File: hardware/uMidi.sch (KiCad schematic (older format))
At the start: 61 parts, among them CON1 USB-MINI-B, IC1 ATXMEGA128A4U-M, IC2 74LS14, IC3 LT1129CST-3.3, IC4 6N138, P1 MIDI In, P2 MIDI Thru, P3 MIDI T/O, P4 MIDI Out, P5 5..12 V, P6 PDI, P7 GPIO1, P8 GPIO2, P9 GPIO3

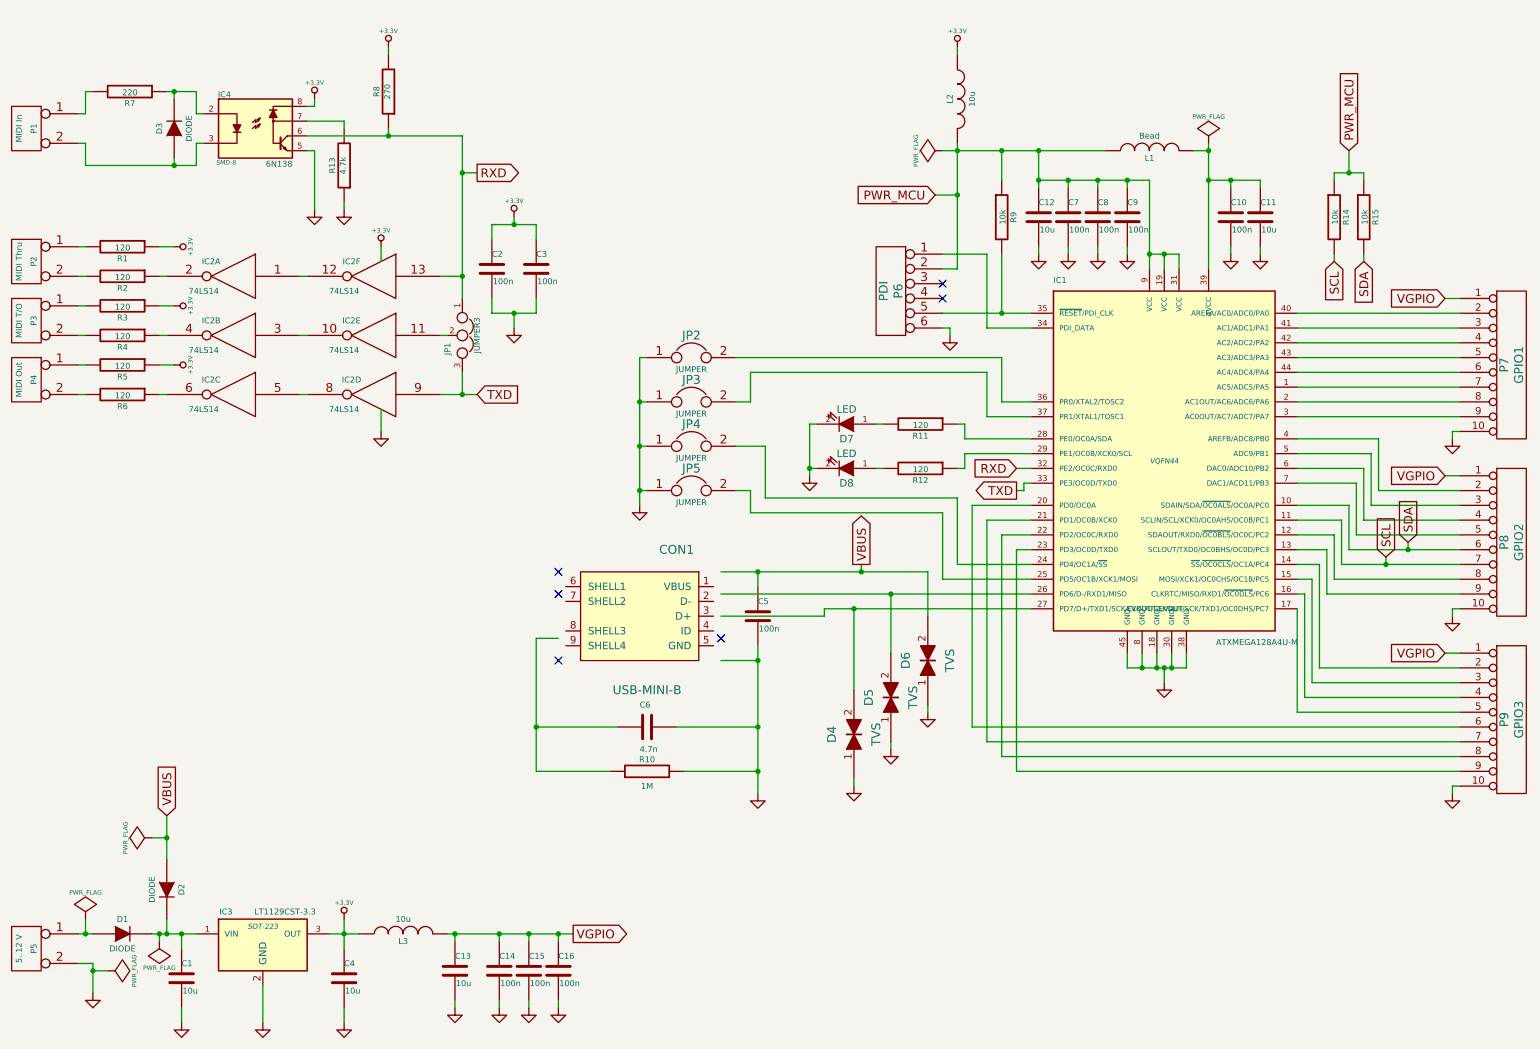
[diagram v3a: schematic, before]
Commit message: Fix usb connector in schematic
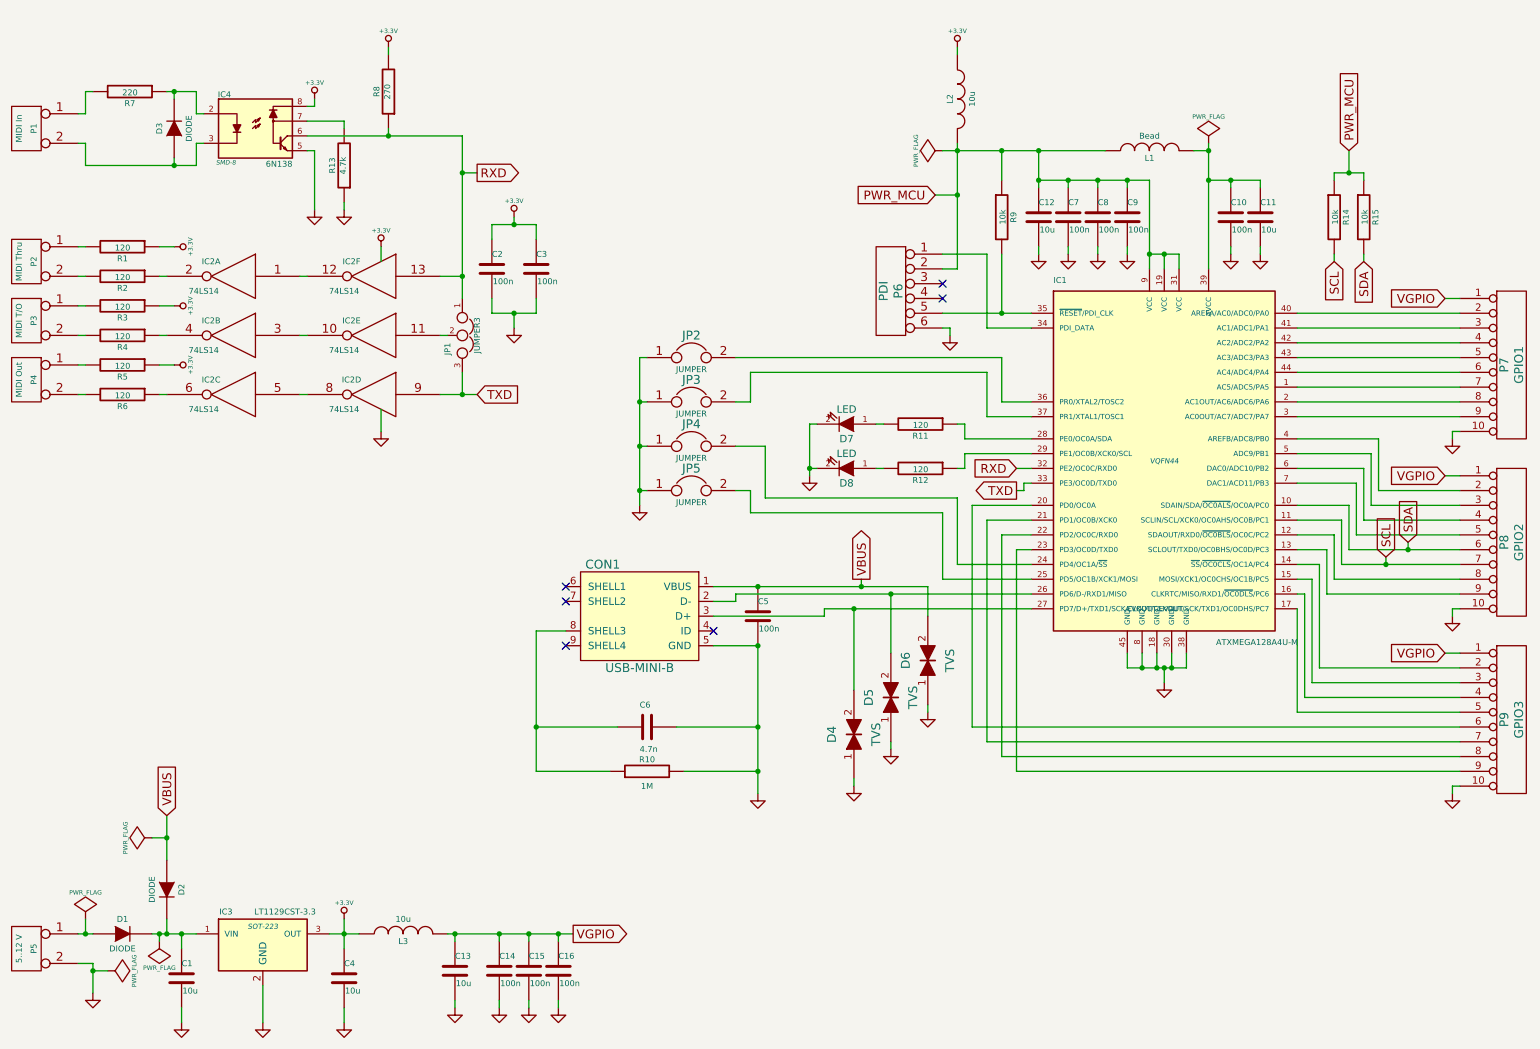
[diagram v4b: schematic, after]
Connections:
- net GND: now also CON1.5 (GND)
- net VBUS: now also CON1.1 (VBUS)
- net at D5.2, IC1.26 (PD6/D-/RXD1/MISO): now also CON1.2 (D-)
- net at D4.2, IC1.27 (PD7/D+/TXD1/SCK/CLKOUT/EVOUT): now also CON1.3 (D+)
- net at CON1.8 (SHELL3): now also C6.2, R10.1
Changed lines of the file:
@@
 U 1 1 53C6D9DB
 P 4950 4600
-F 0 "CON1" H 4700 5050 60  0000 C CNN
-F 1 "USB-MINI-B" H 4900 4100 60  0000 C CNN
+F 0 "CON1" H 5200 4950 60  0000 C CNN
+F 1 "USB-MINI-B" H 4950 4250 60  0000 C CNN
 F 2 "" H 4950 4600 60  0000 C CNN
 F 3 "" H 4950 4600 60  0000 C CNN
@@
 	1    0    0    -1
 $EndComp
-Text GLabel 6450 4250 1    60   Output ~ 0
+Text GLabel 6450 4350 1    60   Output ~ 0
 VBUS
 Text GLabel 1750 5950 1    60   Input ~ 0
@@
 	1    0    0    -1
 $EndComp
-NoConn ~ 5500 4750
+NoConn ~ 5450 4700
 $Comp
 L PWR_FLAG #FLG032
@@
 	6200 4550 7600 4550
 Wire Wire Line
-	5500 4450 7600 4450
+	5600 4450 7600 4450
 Wire Wire Line
 	3750 2950 3750 3100
@@
 	6200 4600 6200 4550
 Wire Wire Line
-	5500 4600 6200 4600
-Wire Wire Line
-	5500 4900 5750 4900
-Wire Wire Line
-	6450 4300 6450 4250
+	5450 4600 6200 4600
+Wire Wire Line
+	5450 4800 5750 4800
+Wire Wire Line
+	6450 4400 6450 4350
 Wire Wire Line
 	7600 4150 7500 4150
@@
 Wire Wire Line
 	7050 2650 7050 2700
-Connection ~ 6450 4300
+Connection ~ 6450 4400
 Connection ~ 6650 4450
 Connection ~ 6400 4550
@@
 	6650 4450 6650 4850
 Wire Wire Line
-	6900 4300 6900 4600
+	6900 4400 6900 4600
 Wire Wire Line
 	5750 4800 5750 5800
-Connection ~ 5750 4900
-Wire Wire Line
-	5750 4400 5750 4300
-Connection ~ 5750 4300
+Connection ~ 5750 4800
+Wire Wire Line
+	5450 4400 6900 4400
+Connection ~ 5750 4400
 Wire Wire Line
 	1250 7000 1350 7000
@@
 	3200 2100 3200 2200
 Wire Wire Line
-	4400 4750 4250 4750
-Wire Wire Line
-	4250 4750 4250 5650
+	4250 4700 4250 5650
 Wire Wire Line
 	4250 5350 4800 5350
@@
 Wire Wire Line
 	9750 1600 9750 1450
-Wire Wire Line
-	5500 4300 6900 4300
-NoConn ~ 4400 4300
-NoConn ~ 4400 4450
-NoConn ~ 4400 4900
+NoConn ~ 4450 4400
+NoConn ~ 4450 4500
+NoConn ~ 4450 4800
 Wire Wire Line
 	3600 3100 3850 3100
@@
 	3600 2300 3750 2300
 Wire Wire Line
-	3750 1350 2700 1350
+	2700 1350 3750 1350
 $Comp
 L JUMPER JP2
@@
 $EndComp
 Wire Wire Line
-	4950 3850 4950 2850
+	4950 2850 4950 3850
 Wire Wire Line
 	4950 2850 5000 2850
@@
 Wire Wire Line
 	5800 3450 5600 3450
+Wire Wire Line
+	4250 4700 4450 4700
+Wire Wire Line
+	5600 4450 5600 4500
+Wire Wire Line
+	5600 4500 5450 4500
 $EndSCHEMATC

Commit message: Rescue symbols to work with kicad bzr 6188
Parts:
- C1, C10, C11, C12, C13, C14, C15, C16, C2, C3, C4, C5, C6, C7, C8, C9: symbol C -> C-RESCUE-uMidi
- D7, D8: symbol LED -> LED-RESCUE-uMidi
- IC4: symbol 6N135 -> 6N135-RESCUE-uMidi
- R1, R10, R11, R12, R13, R14, R15, R2, R3, R4, R5, R6, R7, R8, R9: symbol R -> R-RESCUE-uMidi
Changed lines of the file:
@@
 EESchema Schematic File Version 2
+LIBS:uMidi-rescue
 LIBS:power
 LIBS:device
@@
 LIBS:memory
 LIBS:xilinx
-LIBS:special
 LIBS:microcontrollers
 LIBS:dsp
@@
 LIBS:atmel
 LIBS:uMidi-cache
-EELAYER 24 0
+EELAYER 25 0
 EELAYER END
 $Descr A4 11693 8268
@@
 $EndComp
 $Comp
-L +3.3V #PWR02
+L +3.3V-RESCUE-uMidi #PWR02
 U 1 1 53C6C3CA
 P 7100 750
@@
 $EndComp
 $Comp
-L R R9
+L R-RESCUE-uMidi R9
 U 1 1 53C6C462
 P 7400 1900
@@
 $EndComp
 $Comp
-L +3.3V #PWR05
+L +3.3V-RESCUE-uMidi #PWR05
 U 1 1 53C6D766
 P 3200 2100
@@
 $EndComp
 $Comp
-L R R2
+L R-RESCUE-uMidi R2
 U 1 1 53C9474B
 P 1450 2300
@@
 $EndComp
 $Comp
-L R R4
+L R-RESCUE-uMidi R4
 U 1 1 53C94767
 P 1450 2700
@@
 $EndComp
 $Comp
-L R R6
+L R-RESCUE-uMidi R6
 U 1 1 53C94772
 P 1450 3100
@@
 $EndComp
 $Comp
-L R R1
+L R-RESCUE-uMidi R1
 U 1 1 53C9484F
 P 1450 2100
@@
 $EndComp
 $Comp
-L R R3
+L R-RESCUE-uMidi R3
 U 1 1 53C9485A
 P 1450 2500
@@
 $EndComp
 $Comp
-L R R5
+L R-RESCUE-uMidi R5
 U 1 1 53C94865
 P 1450 2900
@@
 $EndComp
 $Comp
-L +3.3V #PWR07
+L +3.3V-RESCUE-uMidi #PWR07
 U 1 1 53C94936
 P 1800 2100
@@
 $EndComp
 $Comp
-L +3.3V #PWR08
+L +3.3V-RESCUE-uMidi #PWR08
 U 1 1 53C94941
 P 1800 2500
@@
 $EndComp
 $Comp
-L +3.3V #PWR09
+L +3.3V-RESCUE-uMidi #PWR09
 U 1 1 53C9494C
 P 1800 2900
@@
 $EndComp
 $Comp
-L 6N135 IC4
+L 6N135-RESCUE-uMidi IC4
 U 1 1 53C94FAA
 P 2350 1300
@@
 $EndComp
 $Comp
-L R R7
+L R-RESCUE-uMidi R7
 U 1 1 53C94FCB
 P 1500 1050
@@
 $EndComp
 $Comp
-L +3.3V #PWR010
+L +3.3V-RESCUE-uMidi #PWR010
 U 1 1 53C95524
 P 2750 1100
@@
 $EndComp
 $Comp
-L R R8
+L R-RESCUE-uMidi R8
 U 1 1 53C9552F
 P 3250 1050
@@
 $EndComp
 $Comp
-L +3.3V #PWR011
+L +3.3V-RESCUE-uMidi #PWR011
 U 1 1 53C956B4
 P 3250 750
@@
 TXD
 $Comp
-L C C7
+L C-RESCUE-uMidi C7
 U 1 1 53CA9538
 P 7850 1900
@@
 $EndComp
 $Comp
-L C C8
+L C-RESCUE-uMidi C8
 U 1 1 53CA95D0
 P 8050 1900
@@
 $EndComp
 $Comp
-L C C9
+L C-RESCUE-uMidi C9
 U 1 1 53CA95DB
 P 8250 1900
@@
 $EndComp
 $Comp
-L C C12
+L C-RESCUE-uMidi C12
 U 1 1 53CA95EC
 P 7650 1900
@@
 $EndComp
 $Comp
-L C C11
+L C-RESCUE-uMidi C11
 U 1 1 53CA9C01
 P 9150 1900
@@
 $EndComp
 $Comp
-L C C10
+L C-RESCUE-uMidi C10
 U 1 1 53CA9C0C
 P 8950 1900
@@
 $EndComp
 $Comp
-L C C4
+L C-RESCUE-uMidi C4
 U 1 1 53CABAC9
 P 2950 7050
@@
 $EndComp
 $Comp
-L +3.3V #PWR021
+L +3.3V-RESCUE-uMidi #PWR021
 U 1 1 53CABBFC
 P 2950 6650
@@
 $EndComp
 $Comp
-L C C1
+L C-RESCUE-uMidi C1
 U 1 1 53CAA38D
 P 1850 7050
@@
 $EndComp
 $Comp
-L C C2
+L C-RESCUE-uMidi C2
 U 1 1 53CAAC0C
 P 3950 2250
@@
 $EndComp
 $Comp
-L C C3
+L C-RESCUE-uMidi C3
 U 1 1 53CAAC17
 P 4250 2250
@@
 $EndComp
 $Comp
-L +3.3V #PWR025
+L +3.3V-RESCUE-uMidi #PWR025
 U 1 1 53CAAF3E
 P 4100 1900
@@
 $EndComp
 $Comp
-L C C5
+L C-RESCUE-uMidi C5
 U 1 1 53CD5DBF
 P 5750 4600
@@
 $EndComp
 $Comp
-L C C6
+L C-RESCUE-uMidi C6
 U 1 1 546CD5B3
 P 5000 5350
@@
 $EndComp
 $Comp
-L R R10
+L R-RESCUE-uMidi R10
 U 1 1 546CD6F8
 P 5000 5650
@@
 $EndComp
 $Comp
-L C C13
+L C-RESCUE-uMidi C13
 U 1 1 546E3C38
 P 3700 7000
@@
 $EndComp
 $Comp
-L C C16
+L C-RESCUE-uMidi C16
 U 1 1 546E3CB6
 P 4400 7000
@@
 $EndComp
 $Comp
-L C C15
+L C-RESCUE-uMidi C15
 U 1 1 546E3D1F
 P 4200 7000
@@
 $EndComp
 $Comp
-L C C14
+L C-RESCUE-uMidi C14
 U 1 1 546E3D7F
 P 4000 7000
@@
 VGPIO
 $Comp
-L R R11
+L R-RESCUE-uMidi R11
 U 1 1 546F0CF2
 P 6850 3300
@@
 $EndComp
 $Comp
-L R R12
+L R-RESCUE-uMidi R12
 U 1 1 546F0E74
 P 6850 3600
@@
 $EndComp
 $Comp
-L LED D7
+L LED-RESCUE-uMidi D7
 U 1 1 546F2E09
 P 6350 3300
@@
 $EndComp
 $Comp
-L LED D8
+L LED-RESCUE-uMidi D8
 U 1 1 546F2EDE
 P 6350 3600
@@
 $EndComp
 $Comp
-L R R13
+L R-RESCUE-uMidi R13
 U 1 1 54705F59
 P 2950 1550
@@
 $EndComp
 $Comp
-L R R14
+L R-RESCUE-uMidi R14
 U 1 1 5484813F
 P 9650 1900
@@
 $EndComp
 $Comp
-L R R15
+L R-RESCUE-uMidi R15
 U 1 1 548484DC
 P 9850 1900

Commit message: Assign some footprints in the schematic
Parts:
- C1, C10, C11, C12, C13, C14, C15, C16, C2, C3, C4, C5, C7, C8, C9, D4, D5, D6, L1, L2, L3: footprint (none) -> Capacitors_SMD:C_0603
- D1, D2, D3: footprint (none) -> SMD:DO-214-AC_SMA
- IC1: footprint VQFN44 -> Atmel:QFN-44-1EP
- IC3: footprint SOT-223 -> SOT223:SOT-223
- IC4: footprint SMD-8 -> Opto:Optocoupler_DIP8_SMD
- P7: footprint (none) -> Connect:VASCH5x2
- P8: value GPIO2 -> GPIO1; footprint (none) -> Connect:VASCH5x2
- P9: value GPIO3 -> GPIO1; footprint (none) -> Connect:VASCH5x2
- R1, R10, R11, R12, R13, R14, R15, R2, R3, R4, R5, R6, R7, R8, R9: footprint (none) -> Resistors_SMD:R_0603

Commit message: Add supplier links
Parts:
- C1, C11, C12, C13, C4: Manufacturer (none) -> Kemet; Manufacturer Part Number (none) -> C0603C106M9PACTU; Supplier (none) -> Digikey; Supplier Link (none) -> https://www.digikey.de/product-detail/de/C0603C106M9PACTU/3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; Supplier Part Number (none) -> 399-5504-1-ND
- C10, C14, C15, C16, C2, C3, C5, C7, C8, C9: Manufacturer (none) -> Samsung; Manufacturer Part Number (none) -> CL10B104KB8NNNC; Supplier (none) -> Digikey; Supplier Link (none) -> https://www.digikey.de/product-detail/de/CL10B104KB8NNNC/12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; Supplier Part Number (none) -> 1276-1000-1-ND
- C6: Manufacturer (none) -> Murata; Manufacturer Part Number (none) -> GRM188R71H472KA01D; Supplier (none) -> Digikey; Supplier Link (none) -> https://www.digikey.de/product-detail/de/GRM188R71H472KA01D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; Supplier Part Number (none) -> 490-1506-1-ND
- CON1: Manufacturer (none) -> Hirose; Manufacturer Part Number (none) -> UX60-MB-5ST; Supplier (none) -> Digikey; Supplier Link (none) -> https://www.digikey.de/product-detail/de/UX60-MB-5ST/H2959C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; Supplier Part Number (none) -> H2959CT-ND
- D1, D2, D3: value DIODE -> B160-13-F; footprint SMD:DO-214-AC_SMA -> SMD:DI-214-AC_SMA; Manufacturer (none) -> Diodes Incorporated; Manufacturer Part Number (none) -> B160-13-F; Supplier (none) -> Digikey; Supplier Link (none) -> https://www.digikey.de/product-detail/de/B160-13-F/B160-FDI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; Supplier Part Number (none) -> B160-FDICT-ND
- D4, D5, D6: value TVS -> TVS 5V; Manufacturer (none) -> Comchip Technology; Manufacturer Part Number (none) -> CPDU5V0; Supplier (none) -> Digikey; Supplier Link (none) -> https://www.digikey.de/product-detail/de/CPDU5V0/641-1088-1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; Supplier Part Number (none) -> 641-1088-1-ND
- D7: value LED -> LED Green; Manufacturer (none) -> Lite-On Inc.; Manufacturer Part Number (none) -> LTST-C191KGKT; Supplier (none) -> Digikey; Supplier Link (none) -> https://www.digikey.de/product-detail/de/LTST-C191KGKT/160-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; Supplier Part Number (none) -> 160-1446-1-ND
- D8: value LED -> LED Red; Manufacturer (none) -> Lite-On Inc.; Manufacturer Part Number (none) -> LTST-C191KRKT; Supplier (none) -> Digikey; Supplier Link (none) -> https://www.digikey.de/product-detail/de/LTST-C191KRKT/160-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; Supplier Part Number (none) -> 160-1447-1-ND
- IC1: Manufacturer (none) -> Atmel; Manufacturer Part Number (none) -> ATXMEGA128A4U-MH; Supplier (none) -> Digikey; Supplier Link (none) -> https://www.digikey.de/product-detail/de/ATXMEGA128A4U-MH/A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; Supplier Part Number (none) -> ATXMEGA128A4U-MH-ND
- IC2: Manufacturer (none) -> NXP; Manufacturer Part Number (none) -> 74LVT14D,118; Supplier (none) -> Digikey; Supplier Link (none) -> https://www.digikey.de/product-detail/de/74LVT14D,118/568-8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; Supplier Part Number (none) -> 568-8193-1-ND
- IC3: Manufacturer (none) -> Linear Technology; Manufacturer Part Number (none) -> LT1129CST-3.3#PBF; Supplier (none) -> Digikey; Supplier Link (none) -> https://www.digikey.de/product-detail/de/LT1129CST-3.3%23PB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; Supplier Part Number (none) -> LT1129CST-3.3#PBF-ND
- IC4: Manufacturer (none) -> Lite-On Inc.; Manufacturer Part Number (none) -> 6N138S-TA1; Supplier (none) -> Digikey; Supplier Link (none) -> https://www.digikey.de/product-detail/de/6N138S-TA1/160-179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; Supplier Part Number (none) -> 160-1798-1-ND
- L1: value Bead -> Bead 1k@100MHz; Manufacturer (none) -> Murata; Manufacturer Part Number (none) -> BLM18RK102SN1D; Supplier (none) -> Digikey; Supplier Link (none) -> https://www.digikey.de/product-detail/de/BLM18RK102SN1D/490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; Supplier Part Number (none) -> 490-5228-1-ND
- L2, L3: Manufacturer (none) -> TDK; Manufacturer Part Number (none) -> GLFR1608T100M-LR; Supplier (none) -> Digikey; Supplier Link (none) -> https://www.digikey.de/product-detail/de/GLFR1608T100M-LR/4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; Supplier Part Number (none) -> 445-3608-1-ND
- P6: Manufacturer (none) -> FCI; Manufacturer Part Number (none) -> 67996-206HLF; Supplier (none) -> Digikey; Supplier Link (none) -> https://www.digikey.de/product-detail/de/67996-206HLF/609-3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; Supplier Part Number (none) -> 609-3210-ND
- P7: Manufacturer (none) -> 3M; Manufacturer Part Number (none) -> 30310-6002HB; Supplier (none) -> Digikey; Supplier Link (none) -> https://www.digikey.de/product-detail/de/30310-6002HB/30310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; Supplier Part Number (none) -> 30310-6002HB-ND
- P8: value GPIO1 -> GPIO2; Manufacturer (none) -> 3M; Manufacturer Part Number (none) -> 30310-6002HB; Supplier (none) -> Digikey; Supplier Link (none) -> https://www.digikey.de/product-detail/de/30310-6002HB/30310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; Supplier Part Number (none) -> 30310-6002HB-ND
- P9: value GPIO1 -> GPIO3; Manufacturer (none) -> 3M; Manufacturer Part Number (none) -> 30310-6002HB; Supplier (none) -> Digikey; Supplier Link (none) -> https://www.digikey.de/product-detail/de/30310-6002HB/30310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; Supplier Part Number (none) -> 30310-6002HB-ND
- R1, R11, R12, R2, R3, R4, R5, R6: Manufacturer (none) -> Panasonic; Manufacturer Part Number (none) -> ERJ-3GEYJ121V; Supplier (none) -> Digikey; Supplier Link (none) -> https://www.digikey.de/product-detail/de/ERJ-3GEYJ121V/P120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; Supplier Part Number (none) -> P120GCT-ND
- R10: Manufacturer (none) -> Panasonic; Manufacturer Part Number (none) -> ERJ-3GEYJ105V; Supplier (none) -> Digikey; Supplier Link (none) -> https://www.digikey.de/product-detail/de/ERJ-3GEYJ105V/P1.0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; Supplier Part Number (none) -> P1.0MGCT-ND
- R13: Manufacturer (none) -> Panasonic; Manufacturer Part Number (none) -> ERJ-3GEYJ472V; Supplier (none) -> Digikey; Supplier Link (none) -> https://www.digikey.de/product-detail/de/ERJ-3GEYJ472V/P4.7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; Supplier Part Number (none) -> P4.7KGCT-ND
- R14, R15, R9: Manufacturer (none) -> Panasonic; Manufacturer Part Number (none) -> ERJ-3GEYJ103V; Supplier (none) -> Digikey; Supplier Link (none) -> https://www.digikey.de/product-detail/de/ERJ-3GEYJ103V/P10K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; Supplier Part Number (none) -> P10KGCT-ND
- R7: Manufacturer (none) -> Panasonic; Manufacturer Part Number (none) -> ERJ-3GEYJ221V; Supplier (none) -> Digikey; Supplier Link (none) -> https://www.digikey.de/product-detail/de/ERJ-3GEYJ221V/P220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; Supplier Part Number (none) -> P220GCT-ND
- R8: Manufacturer (none) -> Panasonic; Manufacturer Part Number (none) -> ERJ-3GEYJ271V; Supplier (none) -> Digikey; Supplier Link (none) -> https://www.digikey.de/product-detail/de/ERJ-3GEYJ271V/P270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; Supplier Part Number (none) -> P270GCT-ND
